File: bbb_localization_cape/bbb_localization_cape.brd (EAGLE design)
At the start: 71.8 x 54.6 mm, 31 parts, among them J1 CONN_04, J2 MOLEX-22-03-5035, U1 SN65HVD256DR, U2 ARDUCAMOV5642, U3 MSP430G2553IPW20R, U4 SN74LV1T126DCKR, U5 SN74LV1T125DCKR, U6 SN74LV1T126DCKR, U7 LP38693MP-3.3/NOPB, U8 LM1085ISX-ADJ

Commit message: Updated pdf and other things
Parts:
- C6: value 100uF -> 47uF

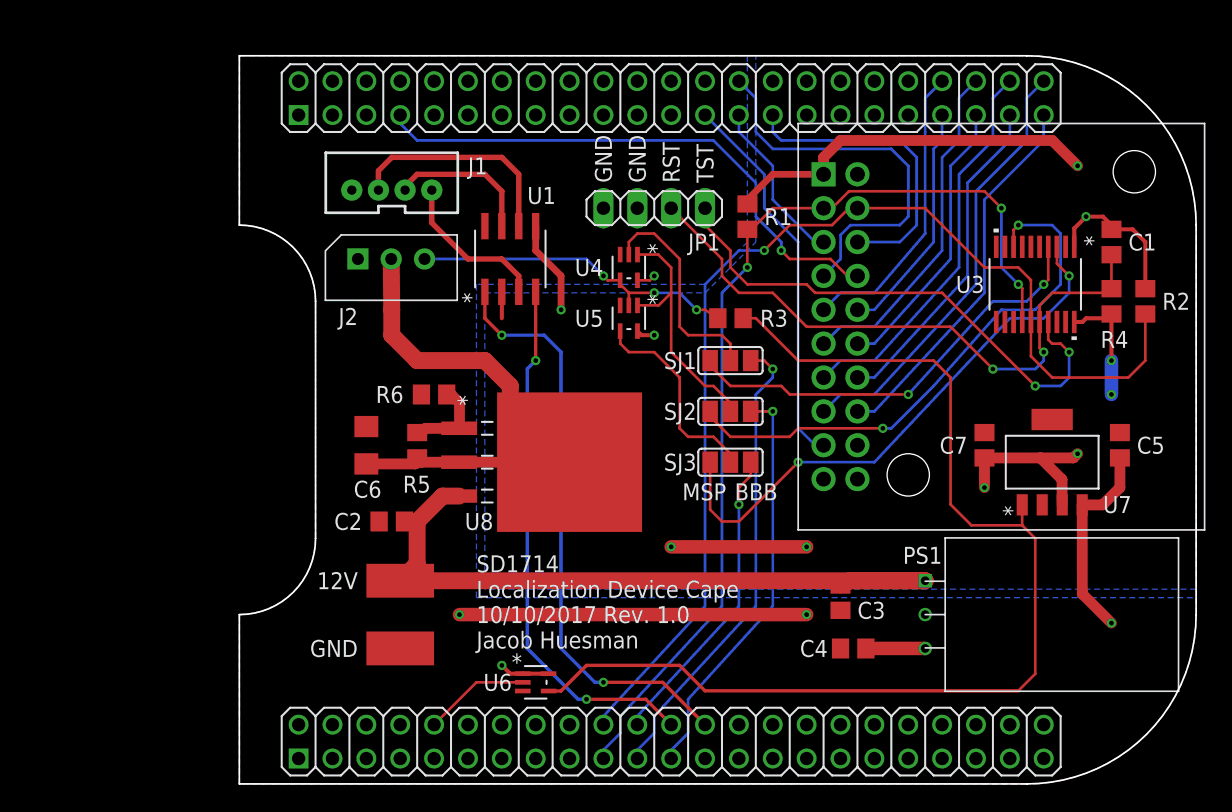
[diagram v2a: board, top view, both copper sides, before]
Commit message: Changed board part from Adafruit to Sparkfun version
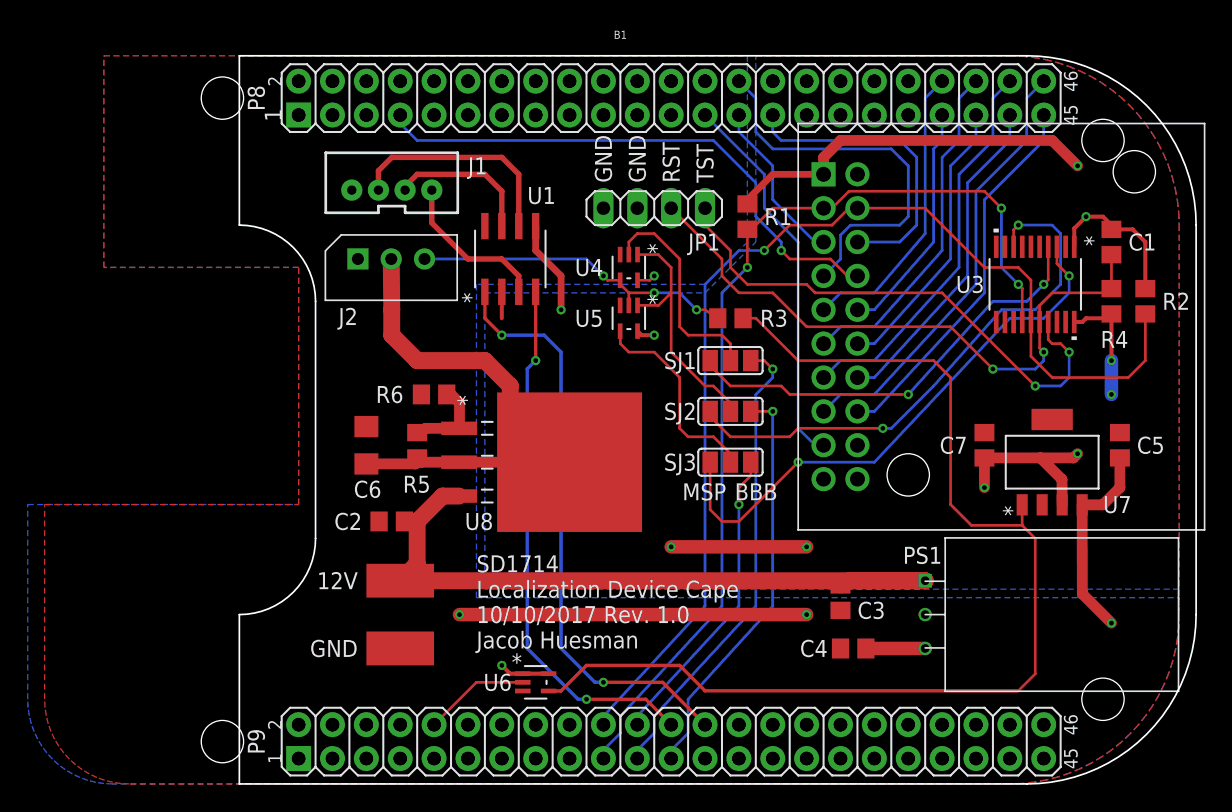
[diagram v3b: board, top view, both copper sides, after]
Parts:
- added B1: SPARKFUN_BEAGLE_BONE_BLACK_CAPE, SparkFun-Boards:BEAGLE_BONE_BLACK_CAPE
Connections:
- net +5V: now also B1.P9.5, B1.P9.6
- net DCAN1_RX: now also B1.P9.24
- net DCAN1_TX: now also B1.P9.26
- net GND: now also B1.P8.1, B1.P8.2, B1.P9.1, B1.P9.2, B1.P9.43, B1.P9.44, B1.P9.45, B1.P9.46
- net I2C2_SCL: now also B1.P9.19
- net I2C2_SDA: now also B1.P9.20
- net PRU1_0: now also B1.P8.45
- net PRU1_1: now also B1.P8.46
- net PRU1_10: now also B1.P8.28
- net PRU1_2: now also B1.P8.43
- net PRU1_3: now also B1.P8.44
- net PRU1_4: now also B1.P8.41
- net PRU1_5: now also B1.P8.42
- net PRU1_6: now also B1.P8.39
- net PRU1_7: now also B1.P8.40
- net PRU1_8: now also B1.P8.27
- net PRU1_9: now also B1.P8.29
- net PWDN: now also B1.P8.25
- net SYS_RESETN: now also B1.P9.10
- net TIMER4: now also B1.P8.7
- net UART2_DIR: now also B1.P9.23
- net UART2_RXD: now also B1.P9.22
- net UART2_TXD: now also B1.P9.21

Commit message: Finished changing cape style
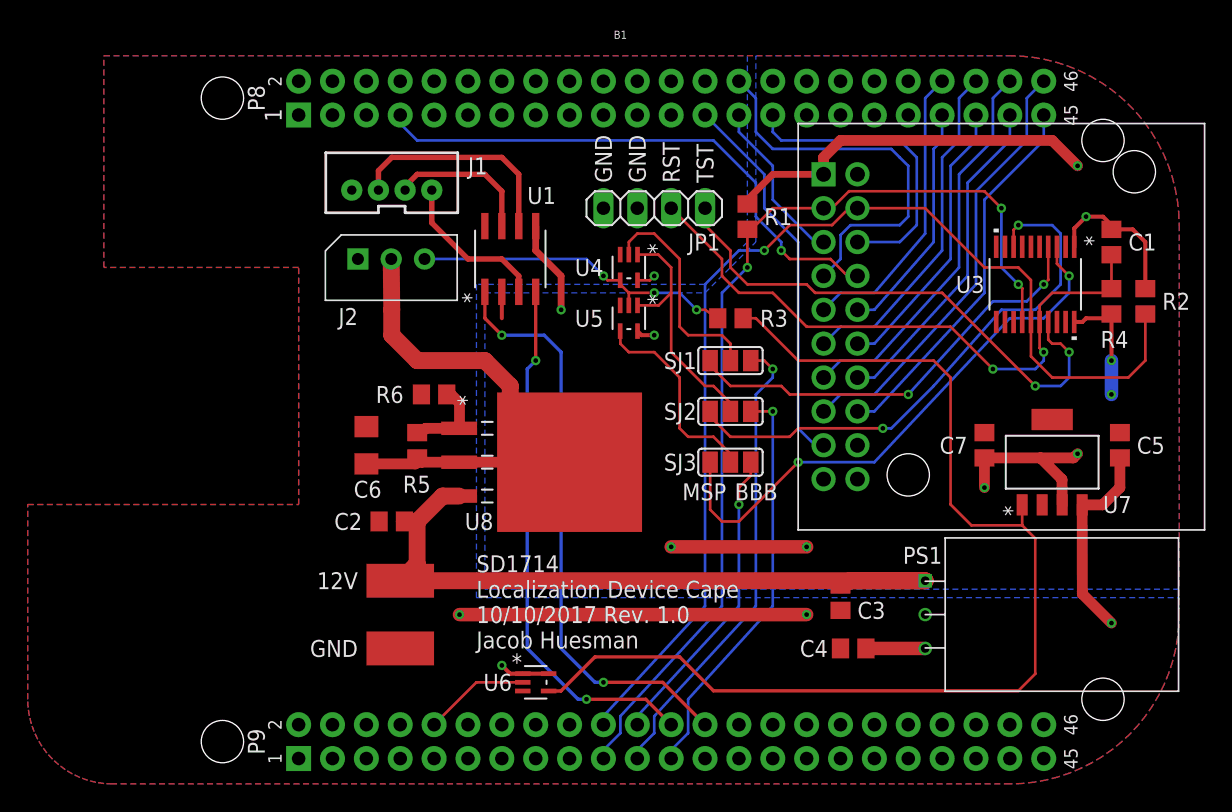
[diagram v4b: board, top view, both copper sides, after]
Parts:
- removed A1: BEAGLEBONE_OUTLINE, bbb_localization_cape:BEAGLEBONE_SHIELD
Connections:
- removed net 03.VDD_3V3: A1.49
- removed net 07.SYS_5V: A1.53
- removed net GNDA_ADC.34: A1.80
- removed net SYS_5V.08: A1.54
- removed net VDD_3V3.04: A1.50
- removed net VDD_ADC.32: A1.78
- net +5V: no longer A1.51, A1.52
- net DCAN1_RX: no longer A1.70
- net DCAN1_TX: no longer A1.72
- net GND: no longer A1.1, A1.2, A1.47, A1.48, A1.89, A1.90, A1.91, A1.92
- net I2C2_SCL: no longer A1.65
- net I2C2_SDA: no longer A1.66
- net PRU1_0: no longer A1.45
- net PRU1_1: no longer A1.46
- net PRU1_10: no longer A1.28
- net PRU1_2: no longer A1.43
- net PRU1_3: no longer A1.44
- net PRU1_4: no longer A1.41
- net PRU1_5: no longer A1.42
- net PRU1_6: no longer A1.39
- net PRU1_7: no longer A1.40
- net PRU1_8: no longer A1.27
- net PRU1_9: no longer A1.29
- net PWDN: no longer A1.25
- net SYS_RESETN: no longer A1.56
- net TIMER4: no longer A1.7
- net UART2_DIR: no longer A1.69
- net UART2_RXD: no longer A1.68
- net UART2_TXD: no longer A1.67
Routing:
- net SYS_RESETN_5V: track 84.6 -> 85.2 mm
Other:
- board outline removed

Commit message: Added reverse current protection and changed PWDN pin
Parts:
- added D1: (no value), diode:DO-214AC
- C6: value 47uF -> 100uF; device rcl:C1206 -> resistor:PANASONIC_E
- moved PAD2 19.1 mm to (7.62, 10.8)
- moved PAD1 19.1 mm to (7.62, 15.2)
- moved R6 14.5 mm to (20.3, 17.8), turned to 90 degrees
- moved U8 14.1 mm to (26.0, 28.6), turned to 0 degrees
- moved C6 13.4 mm to (37.5, 24.8), turned to 180 degrees
- moved R5 9.44 mm to (24.8, 16.5), turned to 0 degrees
- moved PS1 8.89 mm to (57.1, 12.7)
- moved C4 6.48 mm to (54.3, 8.89)
- moved C3 6.35 mm to (53.3, 14.0)
- moved C2 5.71 mm to (31.8, 19.7), turned to 90 degrees
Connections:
- new net N$4: D1.A, PAD1.1
- net +10V: now also C6.+; no longer C6.1
- net +12V: now also D1.C; no longer PAD1.1
- net GND: now also C6.-; no longer C6.2
- net PWDN: now also B1.P8.26; no longer B1.P8.25
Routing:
- net +5V: track 62.8 -> 55.6 mm
- net N$4: track 0.00 -> 6.56 mm
- net +10V: track 37.6 -> 33.4 mm
- net PWDN: track 28.8 -> 31.4 mm
- net +12V: track 55.7 -> 53.8 mm
- net N$3: track 6.42 -> 7.93 mm
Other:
- board text added: "SD1714 Localization Device Cape 10/10/2017 Rev. 1.1 Jacob Huesman"
- board text removed: "SD1714 Localization Device Cape 10/10/2017 Rev. 1.0 Jacob Huesman"

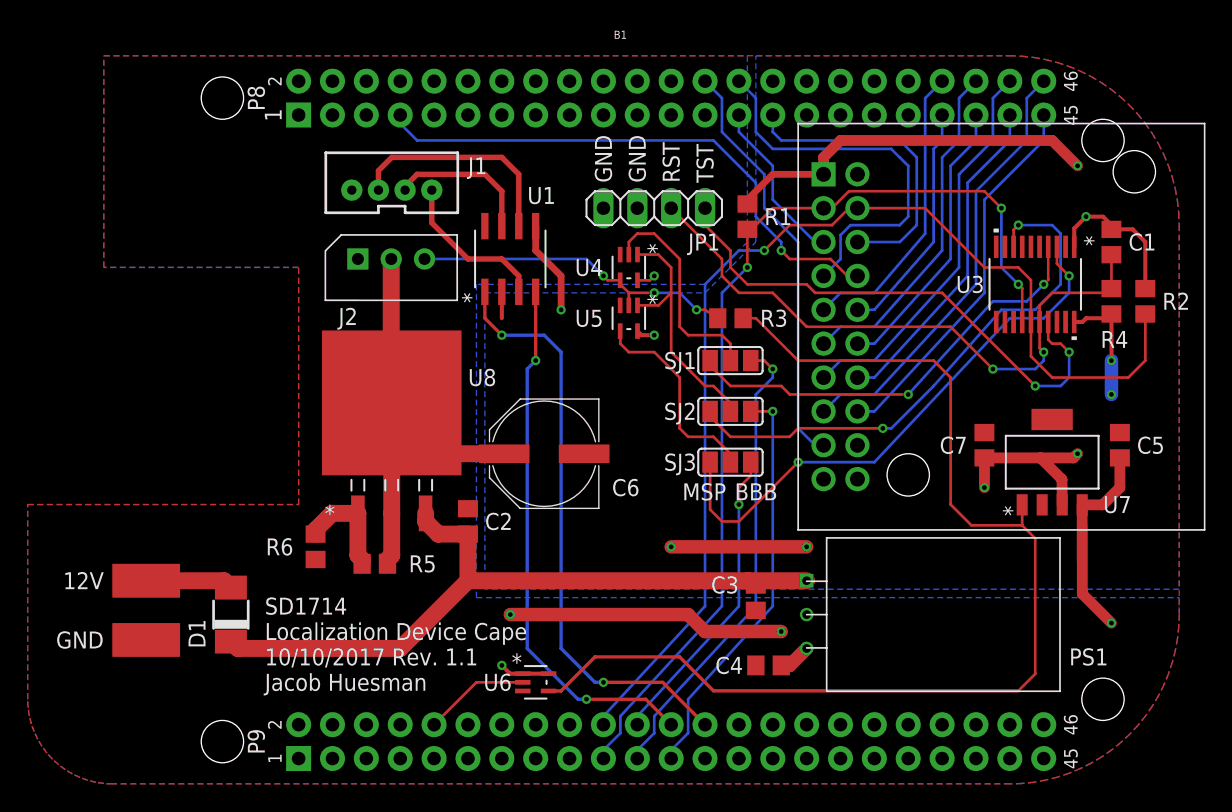
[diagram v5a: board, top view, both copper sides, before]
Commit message: Changed XCLK
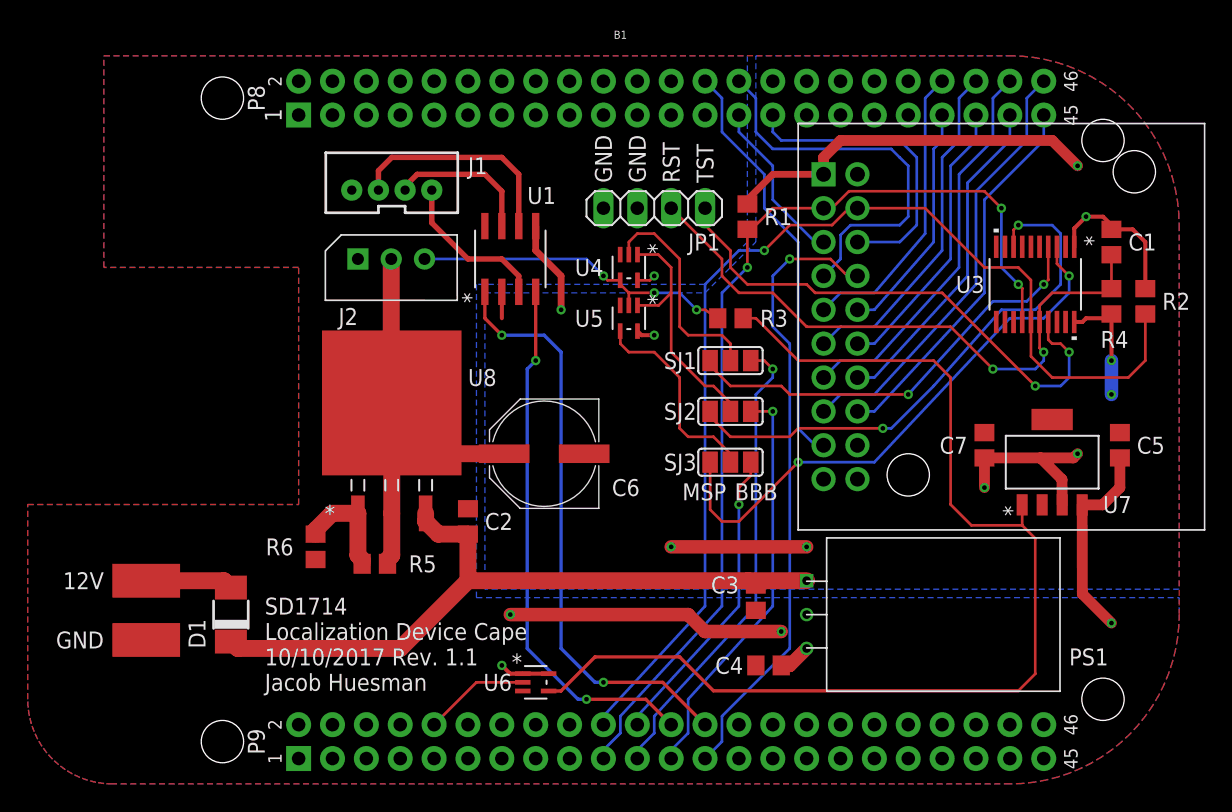
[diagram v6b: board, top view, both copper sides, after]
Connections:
- removed net TIMER4: B1.P8.7, U2.8
- new net XCLK: B1.P9.25, U2.8
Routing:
- net XCLK: track 0.00 -> 46.8 mm, vias 0 -> 1
- net TIMER4: track 41.5 -> 0.00 mm, vias 1 -> 0
- net +10V: track 33.4 -> 38.2 mm
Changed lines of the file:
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@@
 <wire x1="26.035" y1="28.575" x2="26.035" y2="27.94" width="1.27" layer="1"/>
 <wire x1="26.035" y1="27.94" x2="29.21" y2="24.765" width="1.27" layer="1"/>
-<wire x1="29.21" y1="24.765" x2="34.465" y2="24.765" width="1.27" layer="1"/>
-<wire x1="25.995" y1="39.37" x2="25.995" y2="28.615" width="1.27" layer="1"/>
+<wire x1="25.995" y1="28.615" x2="25.995" y2="39.37" width="1.27" layer="1"/>
 <wire x1="25.995" y1="28.615" x2="26.035" y2="28.575" width="1.27" layer="1"/>
+<wire x1="34.465" y1="24.765" x2="29.845" y2="24.765" width="1.27" layer="1"/>
+<wire x1="29.845" y1="24.765" x2="25.995" y2="28.615" width="1.27" layer="1"/>
 </signal>
 <signal name="+3V3">
@@
 <contactref element="B1" pad="P8.39"/>
 </signal>
-<signal name="TIMER4" class="1">
-<contactref element="U2" pad="8"/>
-<wire x1="26.67" y1="50.165" x2="26.67" y2="49.53" width="0.2032" layer="16"/>
-<wire x1="60.96" y1="38.1" x2="60.20983125" y2="38.1" width="0.2032" layer="1"/>
-<wire x1="60.20983125" y1="38.1" x2="58.94423125" y2="39.3656" width="0.2032" layer="1"/>
-<wire x1="55.8844" y1="39.3656" x2="55.245" y2="40.005" width="0.2032" layer="1"/>
-<wire x1="58.94423125" y1="39.3656" x2="55.8844" y2="39.3656" width="0.2032" layer="1"/>
-<via x="55.245" y="40.005" extent="1-16" drill="0.35"/>
-<wire x1="55.245" y1="40.005" x2="55.245" y2="40.64" width="0.2032" layer="16"/>
-<wire x1="55.245" y1="40.64" x2="53.34" y2="42.545" width="0.2032" layer="16"/>
-<wire x1="53.34" y1="42.545" x2="53.34" y2="45.085" width="0.2032" layer="16"/>
-<wire x1="53.34" y1="45.085" x2="50.165" y2="48.26" width="0.2032" layer="16"/>
-<wire x1="50.165" y1="48.26" x2="27.94" y2="48.26" width="0.2032" layer="16"/>
-<wire x1="27.94" y1="48.26" x2="26.67" y2="49.53" width="0.2032" layer="16"/>
-<contactref element="B1" pad="P8.7"/>
-</signal>
 <signal name="PRU1_9" class="1">
 <wire x1="54.61" y1="50.165" x2="54.61" y2="48.895" width="0.2032" layer="16"/>
@@
 <wire x1="13.455" y1="15.24" x2="13.97" y2="14.725" width="1.27" layer="1"/>
 </signal>
+<signal name="XCLK">
+<contactref element="B1" pad="P9.25"/>
+<contactref element="U2" pad="8"/>
+<wire x1="60.20983125" y1="38.1" x2="60.96" y2="38.1" width="0.2032" layer="1"/>
+<wire x1="49.53" y1="1.905" x2="50.8" y2="3.175" width="0.2032" layer="16"/>
+<wire x1="50.8" y1="3.175" x2="50.8" y2="5.08" width="0.2032" layer="16"/>
+<wire x1="50.8" y1="5.08" x2="55.88" y2="10.16" width="0.2032" layer="16"/>
+<wire x1="55.88" y1="33.02" x2="54.61" y2="34.29" width="0.2032" layer="16"/>
+<wire x1="54.61" y1="34.29" x2="54.61" y2="38.1" width="0.2032" layer="16"/>
+<wire x1="55.88" y1="10.16" x2="55.88" y2="33.02" width="0.2032" layer="16"/>
+<wire x1="54.61" y1="38.1" x2="55.88" y2="39.37" width="0.2032" layer="16"/>
+<via x="55.88" y="39.37" extent="1-16" drill="0.35"/>
+<wire x1="55.88" y1="39.37" x2="58.93983125" y2="39.37" width="0.2032" layer="1"/>
+<wire x1="58.93983125" y1="39.37" x2="60.20983125" y2="38.1" width="0.2032" layer="1"/>
+</signal>
 </signals>

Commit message: Added dimension layer
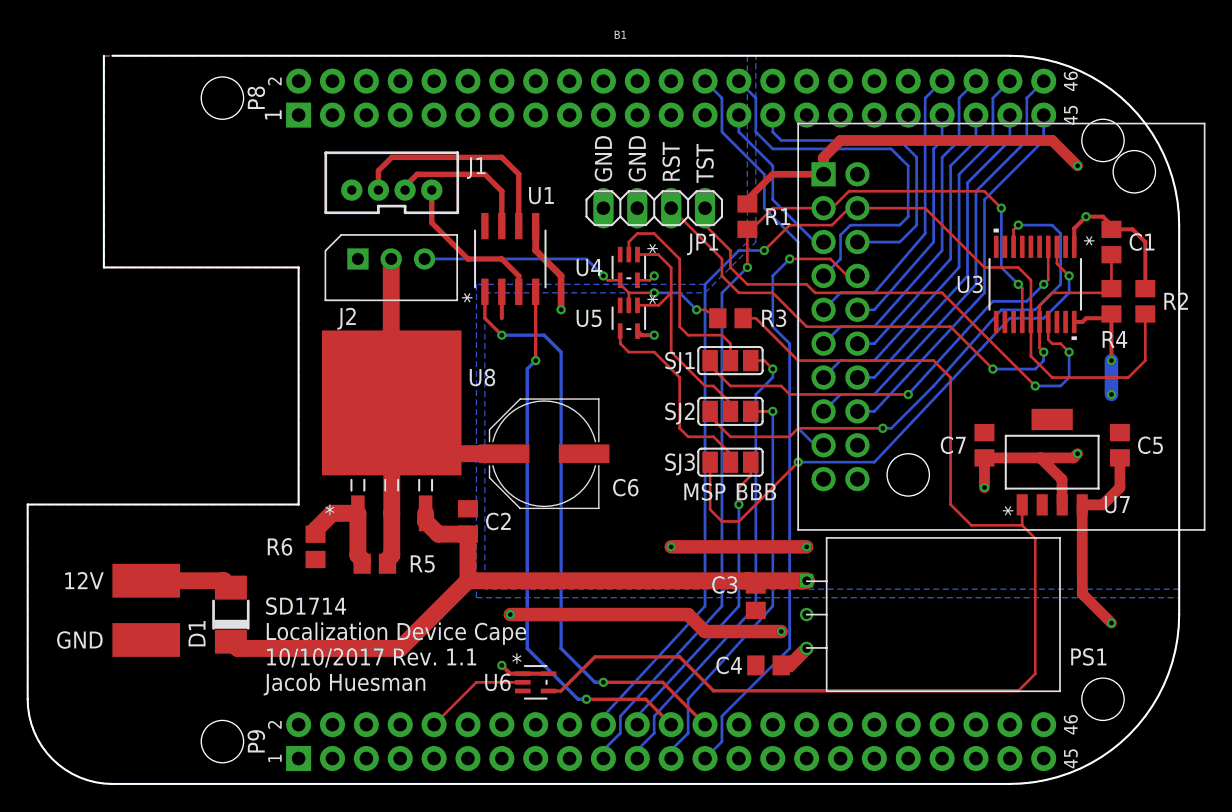
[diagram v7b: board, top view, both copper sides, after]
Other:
- board outline added: 86.4 x 54.6 mm
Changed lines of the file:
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@@
 <text x="48.895" y="28.575" size="1.27" layer="25" rot="R180">SJ2</text>
 <text x="48.895" y="24.765" size="1.27" layer="25" rot="R180">SJ3</text>
+<wire x1="4.445" y1="54.61" x2="4.445" y2="38.735" width="0.1524" layer="20"/>
+<wire x1="4.445" y1="38.735" x2="19.05" y2="38.735" width="0.1524" layer="20"/>
+<wire x1="19.05" y1="38.735" x2="19.05" y2="20.955" width="0.1524" layer="20"/>
+<wire x1="19.05" y1="20.955" x2="-1.27" y2="20.955" width="0.1524" layer="20"/>
+<wire x1="-1.27" y1="20.955" x2="-1.27" y2="6.35" width="0.1524" layer="20"/>
+<wire x1="-1.27" y1="6.35" x2="5.08" y2="0" width="0.1524" layer="20" curve="90"/>
+<wire x1="5.08" y1="0" x2="72.39" y2="0" width="0.1524" layer="20"/>
+<wire x1="72.39" y1="0" x2="85.09" y2="12.7" width="0.1524" layer="20" curve="90"/>
+<wire x1="85.09" y1="12.7" x2="85.09" y2="41.91" width="0.1524" layer="20"/>
+<wire x1="85.09" y1="41.91" x2="72.39" y2="54.61" width="0.1524" layer="20" curve="90"/>
+<wire x1="72.39" y1="54.61" x2="5.08" y2="54.61" width="0.1524" layer="20"/>
 </plain>
 <attributes>
@@
 <attribute name="NOTES" value="Reduced capacitance from 100uF to 47uF, V2 package should be 1210 or larger" x="37.465" y="24.765" size="1.778" layer="27" rot="R180" display="off"/>
 <attribute name="PN" value="445-8047-1-ND" x="37.465" y="24.765" size="1.778" layer="27" rot="R180" display="off"/>
+<attribute name="SPICEPREFIX" value="C" x="37.465" y="24.765" size="1.778" layer="27" rot="R180" display="off"/>
 <attribute name="VENDOR" value="Digi-Key" x="37.465" y="24.765" size="1.778" layer="27" rot="R180" display="off"/>
 </element>
